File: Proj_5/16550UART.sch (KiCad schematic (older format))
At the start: 10 parts, among them J7 DSUB-9, U14 16550, U51 PAL16L8, U52 74AHC1G02, U53 74LVC1G08, U54 74AHC1G02, U55 max235cpg

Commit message: Last error destroyed
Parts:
- removed U52, U54: 74AHC1G02, symbol 74xGxx:74AHC1G02
- removed U53: 74LVC1G08, symbol 74xGxx:74LVC1G08
- added U52: PAL16L8, symbol Logic_Programmable:PAL16L8
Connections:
- wire segments 53 -> 55
- no-connect marks 32 -> 42
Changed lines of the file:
@@
 Text HLabel 8200 7300 0    50   Input ~ 0
 A3
-Text HLabel 4900 6850 0    50   Input ~ 0
-A4
-Text HLabel 4900 6950 0    50   Input ~ 0
-A5
-Text HLabel 4900 7050 0    50   Input ~ 0
-A6
-Text HLabel 4900 7150 0    50   Input ~ 0
-A7
-Text HLabel 4900 7250 0    50   Input ~ 0
-A8
-Text HLabel 4900 7350 0    50   Input ~ 0
-A9
-Text HLabel 4900 7450 0    50   Input ~ 0
+Text HLabel 4900 9600 0    50   Input ~ 0
 A10
-Text HLabel 4900 7550 0    50   Input ~ 0
+Text HLabel 4900 9500 0    50   Input ~ 0
 A11
-Text HLabel 4900 7650 0    50   Input ~ 0
+Text HLabel 4900 9400 0    50   Input ~ 0
 A12
-Text HLabel 5900 7350 2    50   Input ~ 0
+Text HLabel 4900 9300 0    50   Input ~ 0
 A13
-Text HLabel 5900 7250 2    50   Input ~ 0
+Text HLabel 4900 9200 0    50   Input ~ 0
 A14
-Text HLabel 5900 7150 2    50   Input ~ 0
+Text HLabel 4900 9100 0    50   Input ~ 0
 A15
-Text HLabel 4900 6750 0    50   Input ~ 0
-A0
-$Comp
-L 74xGxx:74AHC1G02 U52
-U 1 1 5EA8FF70
-P 6250 5750
-F 0 "U52" V 6179 5880 50  0000 L CNN
-F 1 "74AHC1G02" V 6270 5880 50  0000 L CNN
-F 2 "" H 6250 5750 50  0001 C CNN
-F 3 "http://www.ti.com/lit/sg/scyt129e/scyt129e.pdf" H 6250 5750 50  0001 C CNN
-	1    6250 5750
-	0    1    1    0
-$EndComp
-$Comp
-L 74xGxx:74AHC1G02 U54
-U 1 1 5EA96A09
-P 6950 5750
-F 0 "U54" V 6879 5880 50  0000 L CNN
-F 1 "74AHC1G02" V 6970 5880 50  0000 L CNN
-F 2 "" H 6950 5750 50  0001 C CNN
-F 3 "http://www.ti.com/lit/sg/scyt129e/scyt129e.pdf" H 6950 5750 50  0001 C CNN
-	1    6950 5750
-	0    1    1    0
-$EndComp
-$Comp
-L 74xGxx:74LVC1G08 U53
-U 1 1 5EA99D66
-P 6600 6300
-F 0 "U53" V 6529 6430 50  0000 L CNN
-F 1 "74LVC1G08" V 6620 6430 50  0000 L CNN
-F 2 "" H 6600 6300 50  0001 C CNN
-F 3 "http://www.ti.com/lit/sg/scyt129e/scyt129e.pdf" H 6600 6300 50  0001 C CNN
-	1    6600 6300
-	0    1    1    0
-$EndComp
-Wire Wire Line
-	6650 6000 6950 6000
-Wire Wire Line
-	6550 6000 6250 6000
-Wire Wire Line
-	6600 6550 6600 7050
-Wire Wire Line
-	6600 7050 5900 7050
-Text HLabel 6200 5450 1    50   Input ~ 0
+Text HLabel 4900 9000 0    50   Input ~ 0
 A16
-Text HLabel 6300 5450 1    50   Input ~ 0
+Text HLabel 4900 8900 0    50   Input ~ 0
 A17
-Text HLabel 6900 5450 1    50   Input ~ 0
+Text HLabel 4900 8800 0    50   Input ~ 0
 A18
-Text HLabel 7000 5450 1    50   Input ~ 0
+Text HLabel 4900 8700 0    50   Input ~ 0
 A19
-Wire Wire Line
-	8200 7600 5900 7600
-Wire Wire Line
-	5900 7600 5900 7450
 $Comp
 L power:VCC #PWR092
@@
 	7700 7400 7950 7400
 Connection ~ 7950 7400
-NoConn ~ 5900 6750
 NoConn ~ 5900 6850
 NoConn ~ 5900 6950
@@
 $EndComp
 NoConn ~ 16650 7000
+$Comp
+L Logic_Programmable:PAL16L8 U52
+U 1 1 5EB68290
+P 5400 9200
+F 0 "U52" H 5400 10081 50  0000 C CNN
+F 1 "PAL16L8" H 5400 9990 50  0000 C CNN
+F 2 "" H 5400 9200 50  0001 C CNN
+F 3 "" H 5400 9200 50  0001 C CNN
+	1    5400 9200
+	1    0    0    -1
+$EndComp
+Text HLabel 5900 8800 2    50   Input ~ 0
+A9
+Text HLabel 5900 8900 2    50   Input ~ 0
+A8
+NoConn ~ 5900 9000
+NoConn ~ 5900 9100
+NoConn ~ 5900 9200
+NoConn ~ 5900 9300
+NoConn ~ 5900 9400
+Wire Wire Line
+	5900 8700 5900 8250
+Wire Wire Line
+	5900 8250 4900 8250
+Wire Wire Line
+	4900 8250 4900 7650
+Text HLabel 4900 6750 0    50   Input ~ 0
+A7
+Text HLabel 4900 6850 0    50   Input ~ 0
+A6
+Text HLabel 4900 6950 0    50   Input ~ 0
+A5
+Text HLabel 4900 7050 0    50   Input ~ 0
+A4
+Text HLabel 4900 7150 0    50   Input ~ 0
+A3
+Text HLabel 4900 7250 0    50   Input ~ 0
+A2
+Text HLabel 4900 7350 0    50   Input ~ 0
+A1
+Text HLabel 4900 7450 0    50   Input ~ 0
+A0
+Wire Wire Line
+	5900 6750 7150 6750
+Wire Wire Line
+	7150 6750 7150 7600
+Wire Wire Line
+	7150 7600 8200 7600
+NoConn ~ 5900 7050
+NoConn ~ 5900 7150
+NoConn ~ 5900 7250
+NoConn ~ 5900 7350
+NoConn ~ 5900 7450
+NoConn ~ 4900 7550
+$Comp
+L power:GND #PWR?
+U 1 1 5EB8EA62
+P 5400 9900
+AR Path="/5EAF7226/5EB8EA62" Ref="#PWR?"  Part="1"
+AR Path="/5EA98A67/5EB8EA62" Ref="#PWR0135"  Part="1"
+F 0 "#PWR0135" H 5400 9650 50  0001 C CNN
+F 1 "GND" H 5405 9727 50  0000 C CNN
+F 2 "" H 5400 9900 50  0001 C CNN
+F 3 "" H 5400 9900 50  0001 C CNN
+	1    5400 9900
+	1    0    0    -1
+$EndComp
+Wire Wire Line
+	5400 9800 5400 9900
+$Comp
+L power:VCC #PWR0136
+U 1 1 5EB90779
+P 4750 8500
+F 0 "#PWR0136" H 4750 8350 50  0001 C CNN
+F 1 "VCC" H 4767 8673 50  0000 C CNN
+F 2 "" H 4750 8500 50  0001 C CNN
+F 3 "" H 4750 8500 50  0001 C CNN
+	1    4750 8500
+	1    0    0    -1
+$EndComp
+Wire Wire Line
+	4750 8500 5400 8500
 $EndSCHEMATC

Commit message: Added 5 Footprints
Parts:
- J7: footprint DSUB-9 -> parts:DSUB-9
- U55: footprint max235cpg -> parts:max235cpg
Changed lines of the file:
@@
 F 0 "J7" H 19828 6753 60  0000 L CNN
 F 1 "DSUB-9" H 19828 6647 60  0000 L CNN
-F 2 "DSUB-9" H 19600 6740 60  0001 C CNN
+F 2 "parts:DSUB-9" H 19600 6740 60  0001 C CNN
 F 3 "" H 19000 7100 60  0000 C CNN
 	1    19000 7100
@@
 F 0 "U55" H 15350 7387 60  0000 C CNN
 F 1 "max235cpg" H 15350 7281 60  0000 C CNN
-F 2 "max235cpg" H 15350 7240 60  0001 C CNN
+F 2 "parts:max235cpg" H 15350 7240 60  0001 C CNN
 F 3 "" H 14050 7000 60  0000 C CNN
 	1    14050 7000

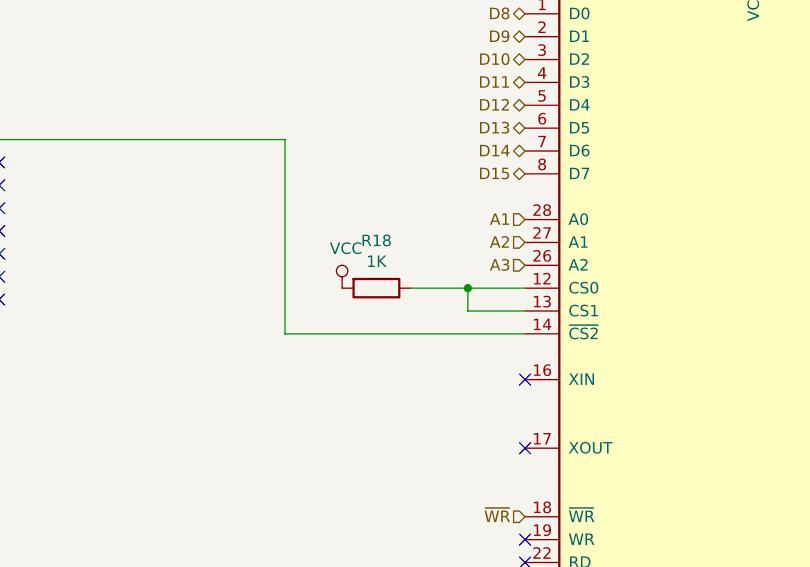
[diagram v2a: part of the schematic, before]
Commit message: Added at least 4 Footprints
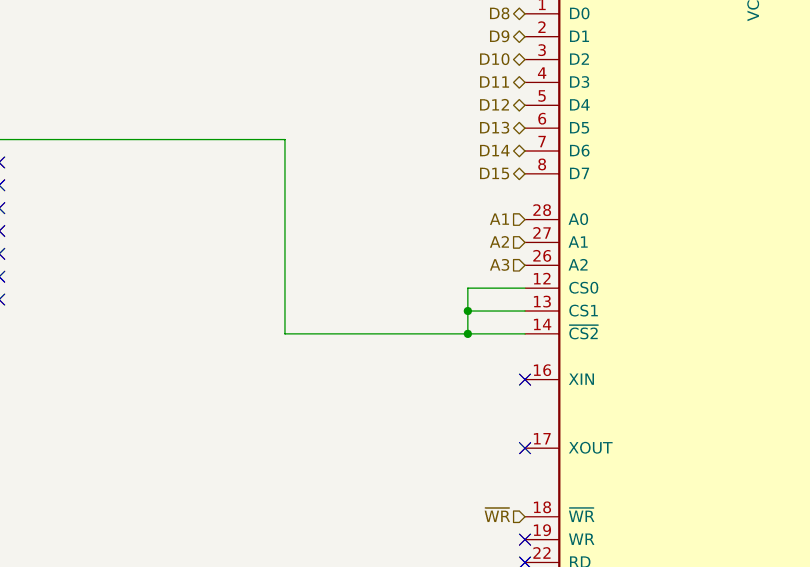
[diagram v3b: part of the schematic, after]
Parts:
- removed R18: 1K, symbol Device:R
- C10, C20: footprint (none) -> Capacitor_Tantalum_SMD:CP_EIA-1608-08_AVX-J
- U51, U52: footprint (none) -> Package_DIP:DIP-20_W7.62mm
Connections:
- net at U14.14 (~CS2~), U51.19 (IO1): now also U14.12 (CS0), U14.13 (CS1)
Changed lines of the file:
@@
 F 0 "C10" V 10248 5650 50  0000 C CNN
 F 1 "0.1uF" V 10339 5650 50  0000 C CNN
-F 2 "" H 10538 5500 50  0001 C CNN
+F 2 "Capacitor_Tantalum_SMD:CP_EIA-1608-08_AVX-J" H 10538 5500 50  0001 C CNN
 F 3 "~" H 10500 5650 50  0001 C CNN
 	1    10500 5650
@@
 F 0 "C20" V 15698 8600 50  0000 C CNN
 F 1 "0.1uF" V 15789 8600 50  0000 C CNN
-F 2 "" H 15988 8450 50  0001 C CNN
+F 2 "Capacitor_Tantalum_SMD:CP_EIA-1608-08_AVX-J" H 15988 8450 50  0001 C CNN
 F 3 "~" H 15950 8600 50  0001 C CNN
 	1    15950 8600
@@
 F 0 "U51" H 5400 8131 50  0000 C CNN
 F 1 "PAL16L8" H 5400 8040 50  0000 C CNN
-F 2 "" H 5400 7250 50  0001 C CNN
+F 2 "Package_DIP:DIP-20_W7.62mm" H 5400 7250 50  0001 C CNN
 F 3 "" H 5400 7250 50  0001 C CNN
 	1    5400 7250
@@
 Text HLabel 4900 8700 0    50   Input ~ 0
 A19
-$Comp
-L power:VCC #PWR092
-U 1 1 5EAA2831
-P 7400 7400
-F 0 "#PWR092" H 7400 7250 50  0001 C CNN
-F 1 "VCC" H 7417 7573 50  0000 C CNN
-F 2 "" H 7400 7400 50  0001 C CNN
-F 3 "" H 7400 7400 50  0001 C CNN
-	1    7400 7400
-	1    0    0    -1
-$EndComp
 Wire Wire Line
 	8200 7400 7950 7400
@@
 Wire Wire Line
 	7950 7500 7950 7400
-$Comp
-L Device:R R18
-U 1 1 5EAA6766
-P 7550 7400
-F 0 "R18" V 7343 7400 50  0000 C CNN
-F 1 "1K" V 7434 7400 50  0000 C CNN
-F 2 "" V 7480 7400 50  0001 C CNN
-F 3 "~" H 7550 7400 50  0001 C CNN
-	1    7550 7400
-	0    1    1    0
-$EndComp
-Wire Wire Line
-	7700 7400 7950 7400
-Connection ~ 7950 7400
 NoConn ~ 5900 6850
 NoConn ~ 5900 6950
@@
 F 0 "U52" H 5400 10081 50  0000 C CNN
 F 1 "PAL16L8" H 5400 9990 50  0000 C CNN
-F 2 "" H 5400 9200 50  0001 C CNN
+F 2 "Package_DIP:DIP-20_W7.62mm" H 5400 9200 50  0001 C CNN
 F 3 "" H 5400 9200 50  0001 C CNN
 	1    5400 9200
@@
 	7150 6750 7150 7600
 Wire Wire Line
-	7150 7600 8200 7600
+	7150 7600 7950 7600
 NoConn ~ 5900 7050
 NoConn ~ 5900 7150
@@
 Wire Wire Line
 	4750 8500 5400 8500
+Wire Wire Line
+	7950 7500 7950 7600
+Connection ~ 7950 7500
+Connection ~ 7950 7600
+Wire Wire Line
+	7950 7600 8200 7600
 $EndSCHEMATC
